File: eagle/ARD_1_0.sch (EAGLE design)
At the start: 13 parts, among them X1 A, X2 B, X3 C, X4 D, X6 ARDUINO_SHIELDNO_SILK, X7 RASPBERRYPI-B+-GPIO

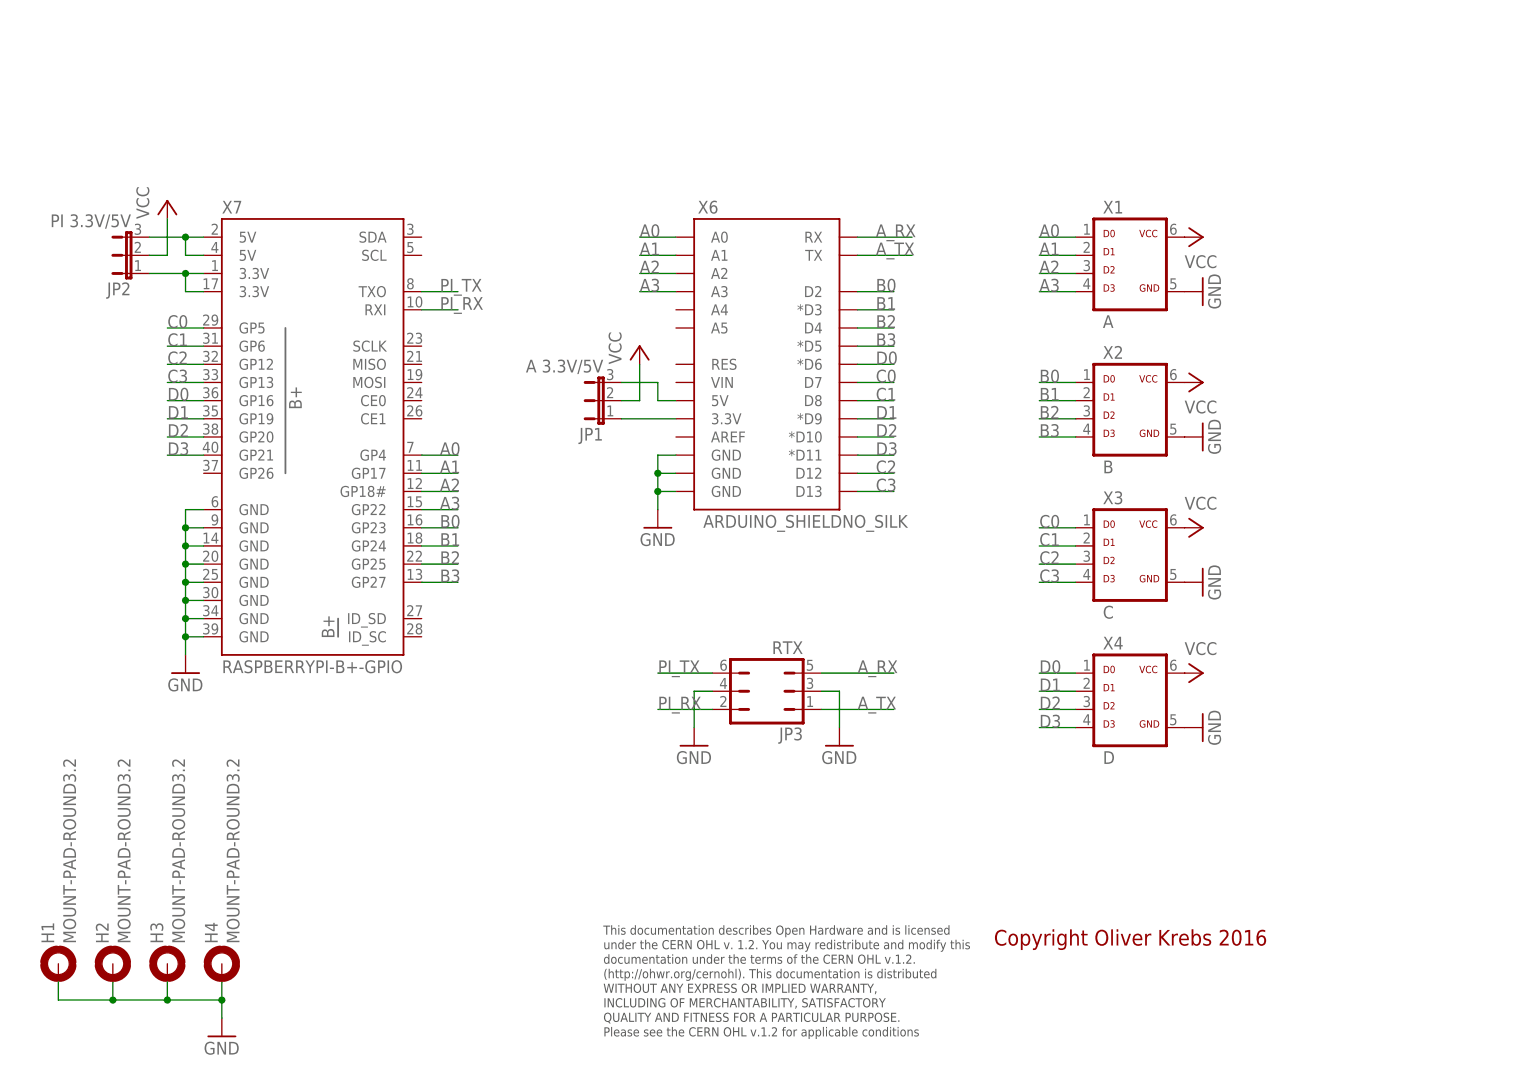
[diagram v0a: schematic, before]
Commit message: Add new tetra-Board and arduino files
Add AMP_1_0, AVC_1_0, D18_1_1, IOP_1_2, MIC_1_0, PIN_1_1, POT_1_0, PWA_1_0, PWR_1_0, RGF 2.0, SOC_2_0, VLT_1_0
Add mex_nano_shield_keyboard, mex_nano_shied_numbers

New arduino projects
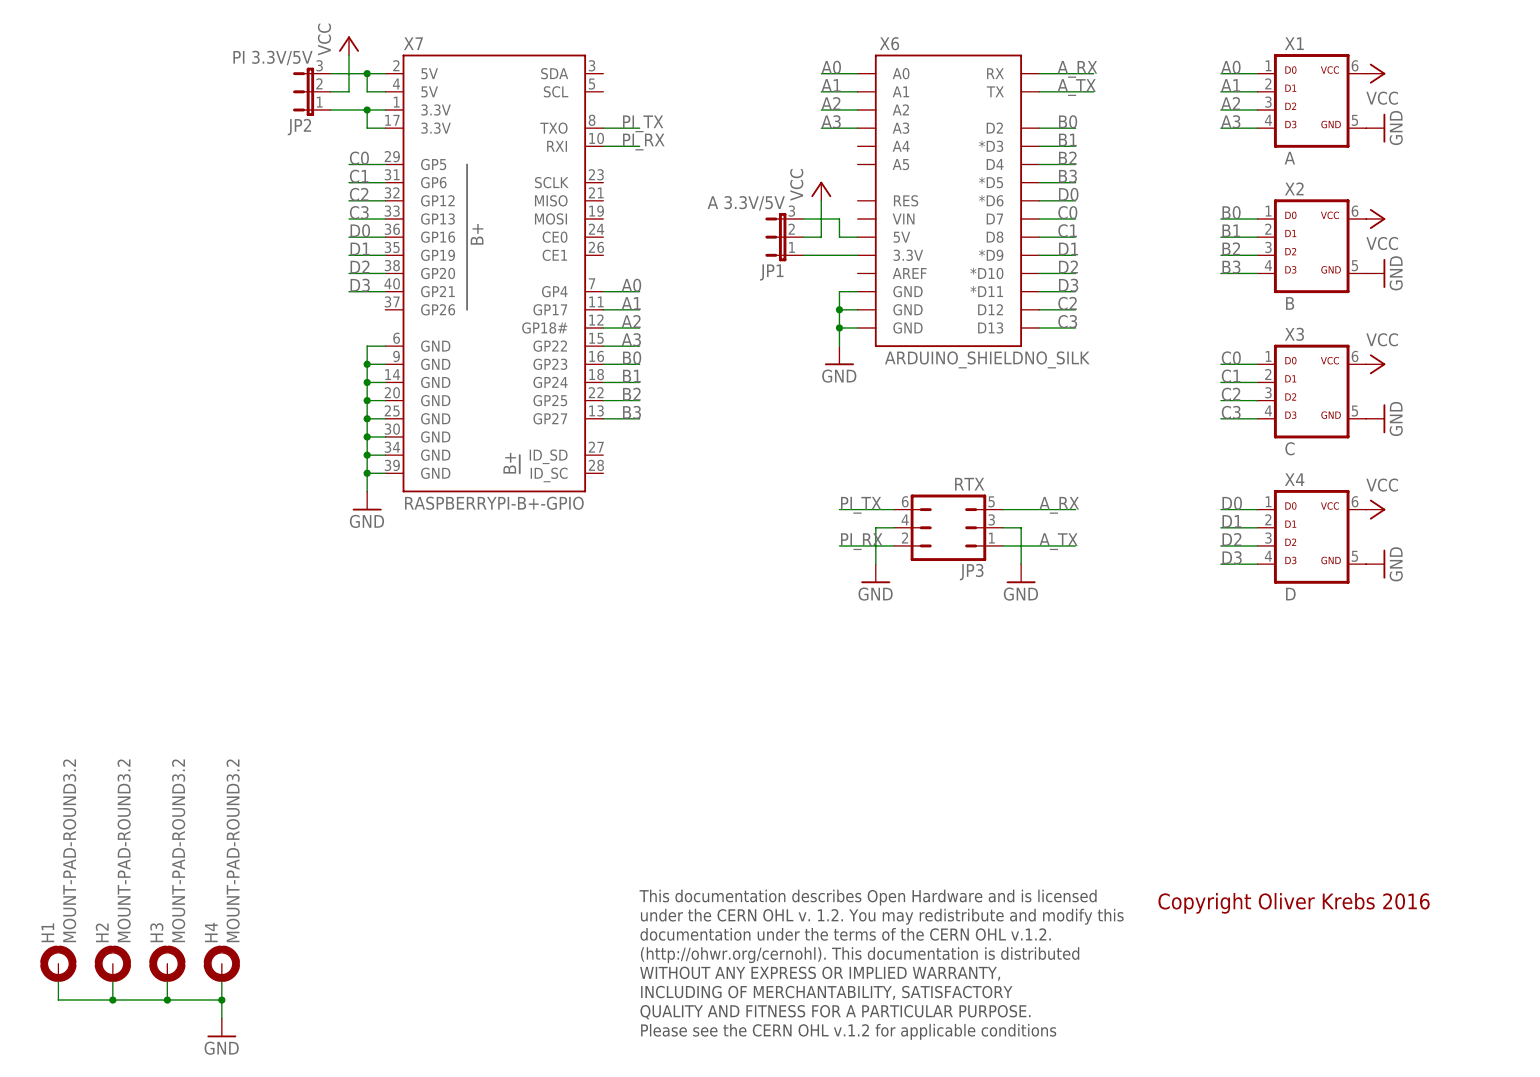
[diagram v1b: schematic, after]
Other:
- moved on the sheet: JP1, JP2, JP3, X1, X2, X3, X4, X6, X7
